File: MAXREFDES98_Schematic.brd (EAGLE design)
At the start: 87.8 x 25.4 mm, 32 parts, among them U1 MB110S-TP, U2 MB110S-TP, U3 MAX5969AETB+

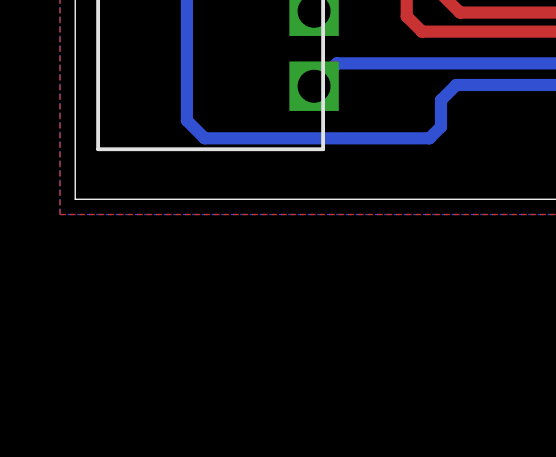
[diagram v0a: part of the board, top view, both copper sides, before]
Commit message: Conneted PG_EN line to SS_INH and added limiting resistors for LEDs
Need to determine if SPD/LNK lines are active high or active low.
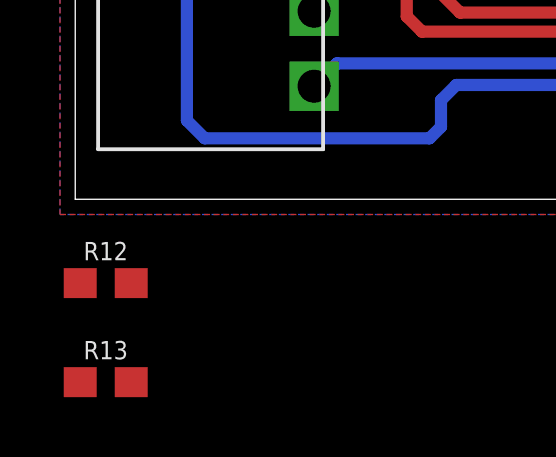
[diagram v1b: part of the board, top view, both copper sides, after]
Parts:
- added R12, R13: 470, SparkFun-Resistors:0603
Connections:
- removed net PG_EN/UVLO: R3.1, U3.8
- removed net SS_INH: C8.1, U$1.3
- new net N$1: D3.A, R12.1
- new net N$2: D4.A, R13.1
- new net PG_EN/SS_INH: C8.1, R3.1, U$1.3, U3.8
- net LNK: now also R12.2; no longer D3.A
- net SPD: now also R13.2; no longer D4.A
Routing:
- net PG_EN/UVLO: track 41.7 -> 0.00 mm, vias 1 -> 0
- net PG_EN/SS_INH: track 0.00 -> 41.7 mm, vias 0 -> 1
- added copper zone on layer 16, net PG_EN/SS_INH
- removed copper zone on layer 16, net PG_EN/UVLO
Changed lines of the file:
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@@
 <attribute name="VALUE" x="93.726" y="3.84175" size="0.6096" layer="27" font="vector" ratio="20" align="top-center"/>
+</element>
+<element name="R12" library="SparkFun-Resistors" library_urn="urn:adsk.eagle:library:532" package="0603" package3d_urn="urn:adsk.eagle:package:39650/1" value="470" x="1.016" y="-2.794" smashed="yes">
+<attribute name="NAME" x="1.016" y="-2.032" size="0.6096" layer="25" font="vector" ratio="20" align="bottom-center"/>
+<attribute name="PROD_ID" value="RES-08609" x="1.143" y="-2.794" size="1.778" layer="27" display="off"/>
+<attribute name="VALUE" x="1.016" y="-3.556" size="0.6096" layer="27" font="vector" ratio="20" align="top-center"/>
+</element>
+<element name="R13" library="SparkFun-Resistors" library_urn="urn:adsk.eagle:library:532" package="0603" package3d_urn="urn:adsk.eagle:package:39650/1" value="470" x="1.016" y="-6.096" smashed="yes">
+<attribute name="NAME" x="1.016" y="-5.334" size="0.6096" layer="25" font="vector" ratio="20" align="bottom-center"/>
+<attribute name="PROD_ID" value="RES-08609" x="1.143" y="-6.096" size="1.778" layer="27" display="off"/>
+<attribute name="VALUE" x="1.016" y="-6.858" size="0.6096" layer="27" font="vector" ratio="20" align="top-center"/>
 </element>
 </elements>
@@
 <wire x1="25.527" y1="10.414" x2="25.527" y2="9.652" width="0.4064" layer="16"/>
 </signal>
-<signal name="PG_EN/UVLO">
+<signal name="PG_EN/SS_INH">
 <contactref element="U3" pad="8"/>
 <contactref element="R3" pad="1"/>
@@
 <wire x1="32.512" y1="8.001" x2="70.993" y2="8.001" width="0.4064" layer="16"/>
 <via x="70.993" y="8.001" extent="1-16" drill="0.35"/>
+<contactref element="U$1" pad="3"/>
+<contactref element="C8" pad="1"/>
+<wire x1="66.3035" y1="18.034" x2="81.827" y2="24.003" width="0" layer="19" extent="1-1"/>
+<wire x1="70.993" y1="8.001" x2="66.3035" y2="18.034" width="0" layer="19" extent="1-1"/>
+<wire x1="29.857" y1="10.0075" x2="30.861" y2="9.906" width="0" layer="19" extent="16-16"/>
 </signal>
 <signal name="5V_OUT">
@@
 <wire x1="81.904" y1="14.859" x2="75.4285" y2="16.764" width="0" layer="19" extent="1-1"/>
 </signal>
-<signal name="SS_INH">
-<contactref element="U$1" pad="3"/>
-<contactref element="C8" pad="1"/>
-<wire x1="81.827" y1="24.003" x2="66.3035" y2="18.034" width="0" layer="19" extent="1-1"/>
-</signal>
 <signal name="BOOT">
 <contactref element="U$1" pad="12"/>
@@
 <signal name="LNK">
 <contactref element="U$2" pad="LNK"/>
-<contactref element="D3" pad="A"/>
-<wire x1="92.304" y1="1.143" x2="70.3228" y2="1.27" width="0" layer="19" extent="1-1"/>
+<contactref element="R12" pad="2"/>
+<wire x1="1.866" y1="-2.794" x2="70.3228" y2="1.27" width="0" layer="19" extent="1-1"/>
 </signal>
 <signal name="SPD">
 <contactref element="U$2" pad="SPD"/>
+<contactref element="R13" pad="2"/>
+<wire x1="1.866" y1="-6.096" x2="72.8628" y2="1.27" width="0" layer="19" extent="1-1"/>
+</signal>
+<signal name="N$1">
+<contactref element="R12" pad="1"/>
+<contactref element="D3" pad="A"/>
+<wire x1="0.166" y1="-2.794" x2="92.304" y2="1.143" width="0" layer="19" extent="1-1"/>
+</signal>
+<signal name="N$2">
+<contactref element="R13" pad="1"/>
 <contactref element="D4" pad="A"/>
-<wire x1="92.304" y1="4.953" x2="72.8628" y2="1.27" width="0" layer="19" extent="1-1"/>
+<wire x1="0.166" y1="-6.096" x2="92.304" y2="4.953" width="0" layer="19" extent="1-1"/>
 </signal>
 </signals>

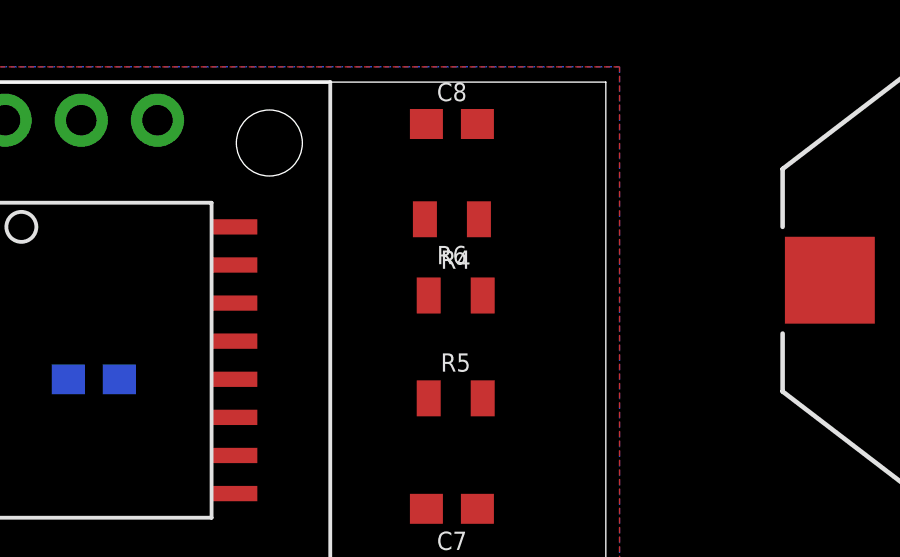
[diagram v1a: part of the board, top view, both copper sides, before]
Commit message: Worked on schematic/checking component values
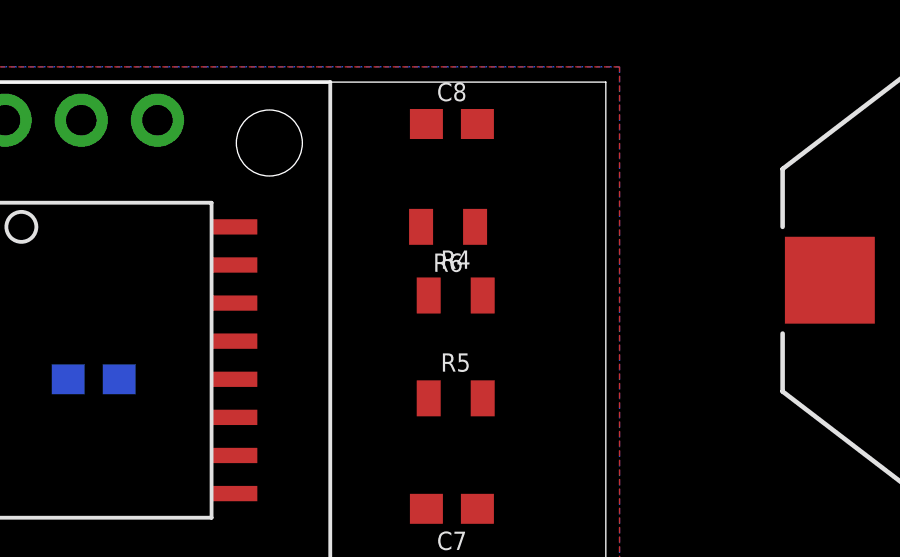
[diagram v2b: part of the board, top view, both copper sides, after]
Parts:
- moved R6 0.28 mm to (82.5, 20.6)
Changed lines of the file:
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@@
 <attribute name="VALUE" x="82.804" y="13.97" size="0.6096" layer="27" font="vector" ratio="20" align="top-center"/>
 </element>
-<element name="R6" library="SparkFun-Resistors" library_urn="urn:adsk.eagle:library:532" package="0805" package3d_urn="urn:adsk.eagle:package:39651/1" value="4.7k" x="82.677" y="20.828" smashed="yes" rot="R180">
-<attribute name="NAME" x="82.677" y="19.939" size="0.6096" layer="25" font="vector" ratio="20" rot="R180" align="bottom-center"/>
-<attribute name="PROD_ID" value="RES-09883" x="82.423" y="20.828" size="1.778" layer="27" rot="R180" display="off"/>
-<attribute name="VALUE" x="82.677" y="21.717" size="0.6096" layer="27" font="vector" ratio="20" rot="R180" align="top-center"/>
+<element name="R6" library="SparkFun-Resistors" library_urn="urn:adsk.eagle:library:532" package="0805" package3d_urn="urn:adsk.eagle:package:39651/1" value="4.7k" x="82.55" y="20.574" smashed="yes" rot="R180">
+<attribute name="NAME" x="82.55" y="19.685" size="0.6096" layer="25" font="vector" ratio="20" rot="R180" align="bottom-center"/>
+<attribute name="PROD_ID" value="RES-09883" x="82.296" y="20.574" size="1.778" layer="27" rot="R180" display="off"/>
+<attribute name="VALUE" x="82.55" y="21.463" size="0.6096" layer="27" font="vector" ratio="20" rot="R180" align="top-center"/>
 </element>
 <element name="R7" library="SparkFun-Resistors" library_urn="urn:adsk.eagle:library:532" package="0805" package3d_urn="urn:adsk.eagle:package:39651/1" value="20k" x="85.852" y="6.096" smashed="yes" rot="R90">
@@
 <contactref element="U$1" pad="14"/>
 <wire x1="81.904" y1="18.288" x2="75.4285" y2="18.034" width="0" layer="19" extent="1-1"/>
-<wire x1="81.777" y1="20.828" x2="81.904" y2="18.288" width="0" layer="19" extent="1-1"/>
+<wire x1="81.65" y1="20.574" x2="81.904" y2="18.288" width="0" layer="19" extent="1-1"/>
 </signal>
 <signal name="GND">
@@
 <wire x1="95.148" y1="1.143" x2="95.148" y2="4.953" width="0" layer="19" extent="1-1"/>
 <wire x1="108.7247" y1="4.826" x2="95.148" y2="1.143" width="0" layer="19" extent="1-1"/>
-<wire x1="83.577" y1="20.828" x2="108.7247" y2="4.826" width="0" layer="19" extent="1-1"/>
-<wire x1="83.527" y1="24.003" x2="83.577" y2="20.828" width="0" layer="19" extent="1-1"/>
+<wire x1="83.45" y1="20.574" x2="108.7247" y2="4.826" width="0" layer="19" extent="1-1"/>
+<wire x1="83.527" y1="24.003" x2="83.45" y2="20.574" width="0" layer="19" extent="1-1"/>
 <wire x1="81.827" y1="11.176" x2="83.527" y2="24.003" width="0" layer="19" extent="1-1"/>
 <wire x1="81.7" y1="7.62" x2="81.827" y2="11.176" width="0" layer="19" extent="1-1"/>

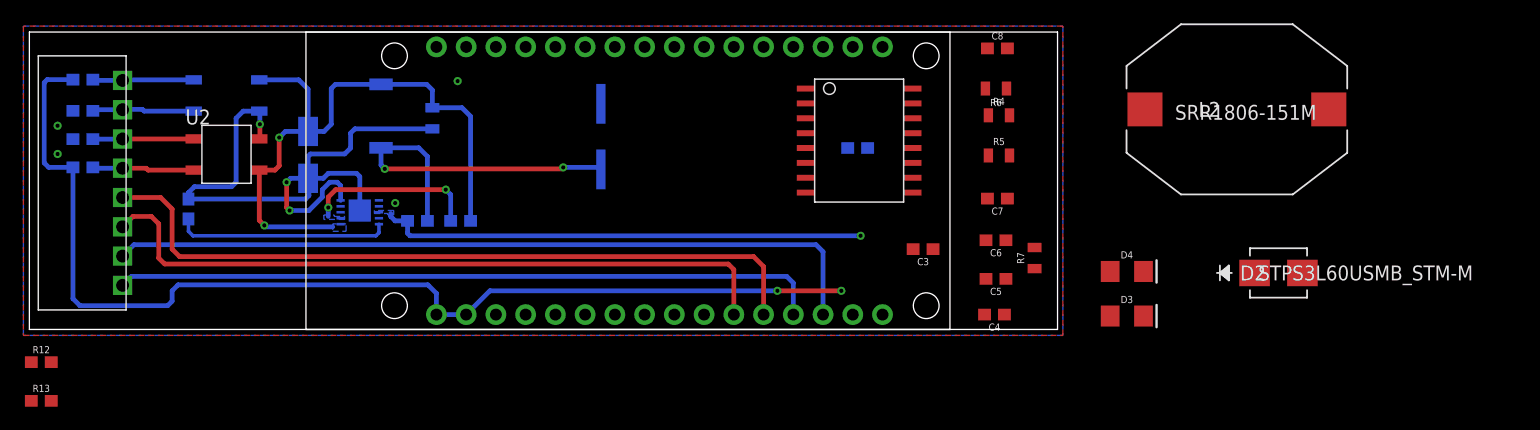
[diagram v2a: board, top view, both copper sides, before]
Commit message: Schematic fixes, parts update, replace parts on board
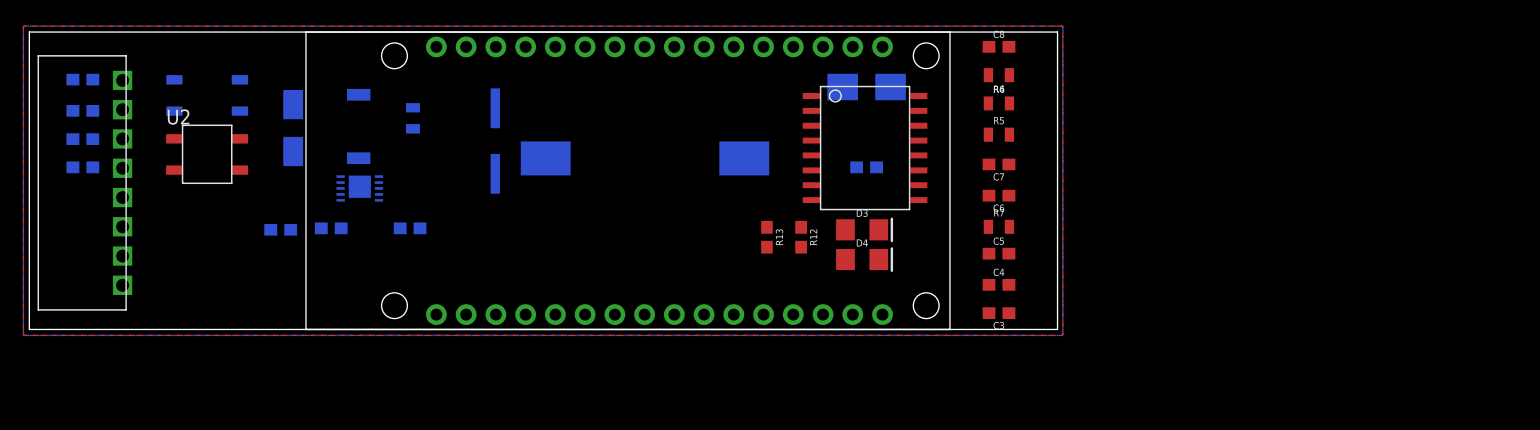
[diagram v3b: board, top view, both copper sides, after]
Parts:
- removed L2: SRR1806-151M, Camera_Board_Parts_09_30_2020:IND_BOURNS_SRR1806
- added L2_150UH: SRR1806-151M, CameraBoard_Library:IND_BOURNS_SRR1806
- moved R12 65.8 mm to (65.9, 7.87), turned to 270 degrees
- moved R13 63.5 mm to (63.0, 7.87), turned to 270 degrees
- moved D2 38.6 mm to (71.5, 20.7), flipped to the bottom, turned to 180 degrees
- moved D3 23.8 mm to (71.1, 8.51)
- moved D4 22.6 mm to (71.1, 5.97)
- moved R2 11.1 mm to (25.8, 8.64)
- moved C2 9.03 mm to (43.9, 11.9)
- moved C3 8.47 mm to (82.8, 1.40)
- moved R1 8.07 mm to (21.5, 8.51), turned to 180 degrees
- moved R7 4.05 mm to (82.8, 8.76), turned to 0 degrees
- moved C6 3.82 mm to (82.8, 11.4)
- moved C7 2.92 mm to (82.8, 14.1)
- moved D1 2.62 mm to (25.8, 20.4)
- moved C4 2.57 mm to (82.8, 3.81), turned to 0 degrees
- moved C5 2.17 mm to (82.8, 6.48), turned to 0 degrees
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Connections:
- net N$8 renamed 3V3
- net 5V_OUT: now also L2_150UH.1; no longer L2.1
- net IND_IN: now also L2_150UH.2; no longer L2.2
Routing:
- net 5V_OUT: track 93.3 -> 0.00 mm, vias 2 -> 0
- net VDD: track 84.4 -> 0.00 mm, vias 4 -> 0
- net TD+: track 65.8 -> 0.00 mm
- net RD+: track 63.3 -> 0.00 mm
- net TD-: track 60.5 -> 0.00 mm
- net VSS_EP: track 60.4 -> 0.00 mm, vias 3 -> 0
- net RD-: track 60.0 -> 0.00 mm
- net PG_EN/SS_INH: track 41.7 -> 0.00 mm, vias 1 -> 0
- net CLS: track 18.3 -> 0.00 mm
- net DET: track 14.8 -> 0.00 mm, vias 2 -> 0
- net RECT1_IN_MINUS: track 8.73 -> 0.00 mm
- net RECT2_IN_PLUS: track 8.71 -> 0.00 mm
- net RECT1_IN_PLUS: track 8.66 -> 0.00 mm
- net RECT2_IN_MINUS: track 8.62 -> 0.00 mm
- removed copper zone on layer 16, net DET
- removed copper zone on layer 16, net PG_EN/SS_INH
- removed copper zone on layer 16, net VDD
